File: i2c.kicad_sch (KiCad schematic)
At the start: 42 parts, among them J12 JST_SH_1x4_BM04B-SRSS-TB-LF-SN, Q22 BSS84AKW, Q24 BSS84AKW, U23 TS5A3359_VSSOP, U24 TS5A3359_VSSOP, U33 TPD4E05U06QDQARQ1, U45 PCA9517ADP, U49 TCA39306_VSSOP

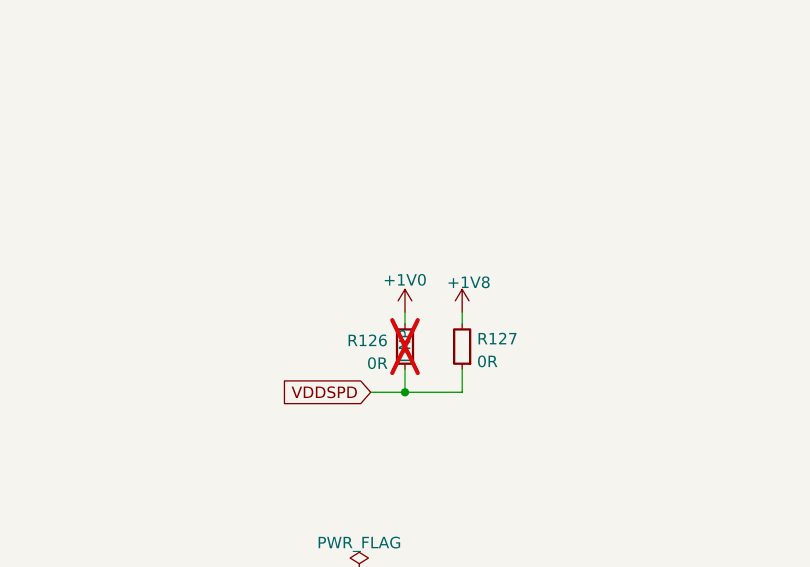
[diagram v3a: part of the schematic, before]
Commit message: [#68199] Start implementing changes after the PCB review
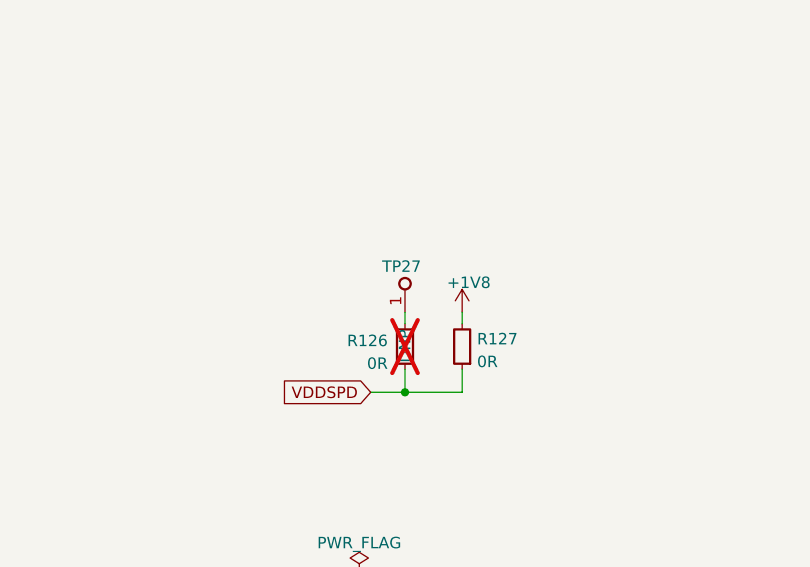
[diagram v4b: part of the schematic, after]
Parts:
- added TP27: TP_0.75mm_SMD, antmicro-footprints:TP_SMD_0.75mm, symbol antmicroTestPoints:TP_0.75mm_SMD
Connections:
- net +1V0: no longer names the net of R126.1
- net +1V0: now also TP27.1
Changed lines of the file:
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@@
+    )
+  )
+  (symbol (lib_id "antmicroTestPoints:TP_0.75mm_SMD") (at 123.19 50.8 90) (unit 1)
+    (in_bom no) (on_board yes) (dnp no)
+    (property "Reference" "TP27" (at 120.65 45.72 90)
+      (effects (font (size 1.27 1.27) (thickness 0.15)) (justify right))
+    )
+    (property "Value" "TP_0.75mm_SMD" (at 127 40.64 0)
+      (effects (font (size 1.27 1.27) (thickness 0.15)) (justify left bottom) hide)
+    )
+    (property "Footprint" "antmicro-footprints:TP_SMD_0.75mm" (at 129.54 40.64 0)
+      (effects (font (size 1.27 1.27) (thickness 0.15)) (justify left bottom) hide)
+    )
+    (property "Datasheet" "" (at 135.89 33.02 0)
+      (effects (font (size 1.27 1.27) (thickness 0.15)) (justify left bottom) hide)
+    )
+    (property "MPN" "" (at 134.62 40.005 0)
+      (effects (font (size 1.27 1.27) (thickness 0.15)) (justify left bottom) hide)
+    )
+    (property "Manufacturer" "" (at 129.54 40.005 0)
+      (effects (font (size 1.27 1.27) (thickness 0.15)) (justify left bottom) hide)
+    )
+    (property "Author" "Antmicro" (at 132.08 40.64 0)
+      (effects (font (size 1.27 1.27) (thickness 0.15)) (justify left bottom) hide)
+    )
+    (property "License" "Apache-2.0" (at 134.62 40.64 0)
+      (effects (font (size 1.27 1.27) (thickness 0.15)) (justify left bottom) hide)
+    )
+    (pin "1")
+    (instances
+      (project "data-center-rdimm-ddr5-tester"
+        (path "/1faa6543-e26a-4449-8bac-ee14b9f19e5f/3f0d6799-172b-44a7-b59e-98d6f5f3049b"
+          (reference "TP27") (unit 1)
+        )
+      )
     )
   )
@@
         )
       )
-    )
-  )
-  (symbol (lib_id "antmicropower:+1V0") (at 123.19 50.8 0) (mirror y) (unit 1)
-    (in_bom yes) (on_board yes) (dnp no) (fields_autoplaced)
-    (property "Reference" "#PWR0272" (at 123.19 54.61 0)
-      (effects (font (size 1.27 1.27)) hide)
-    )
-    (property "Value" "+1V0" (at 123.19 47.244 0)
-      (effects (font (size 1.27 1.27)))
-    )
-    (property "Footprint" "" (at 123.19 50.8 0)
-      (effects (font (size 1.27 1.27)) hide)
-    )
-    (property "Datasheet" "" (at 123.19 50.8 0)
-      (effects (font (size 1.27 1.27)) hide)
-    )
-    (pin "1")
-    (instances
-      (project "data-center-rdimm-ddr5-tester"
-        (path "/1faa6543-e26a-4449-8bac-ee14b9f19e5f/3f0d6799-172b-44a7-b59e-98d6f5f3049b"
-          (reference "#PWR0272") (unit 1)
-        )
-      )
